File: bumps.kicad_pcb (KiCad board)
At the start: 2 copper layers, 111.1 x 65.4 mm, 132 parts, among them M1 CONN_1, M2 CONN_1, M3 CONN_1, P1 DIL6, P10 Mot-A, P11 Mot-A, P12 Mot-X, P13 T1, P14 T2, P15 T3, P16 MPower, P17 PWM-2, P18 PWM-1, P19 END-X, P2 DIL6, P20 END-Y, P21 END-Z, P22 Mot-X, P23 Mot-Y, P24 Mot-Y, P25 Mot-Z, P26 Mot-Z, P27 Aux, P29 PWM, P3 Mot-E, P4 Mot-E, P5 DIL6, P6 DIL6, P7 DIL6, P8 P8 Header, P9 P9 Header, Q1 IRLB8743PBF, Q2 IRLB8743PBF, Q3 FDS9926A, Q4 FDS9926A, U1 E-Polo, U2 A-Polo, U3 X-Polo, U4 Y-Polo, U5 Z-Polo, U6 MC34063, U7 AP1117/3.3

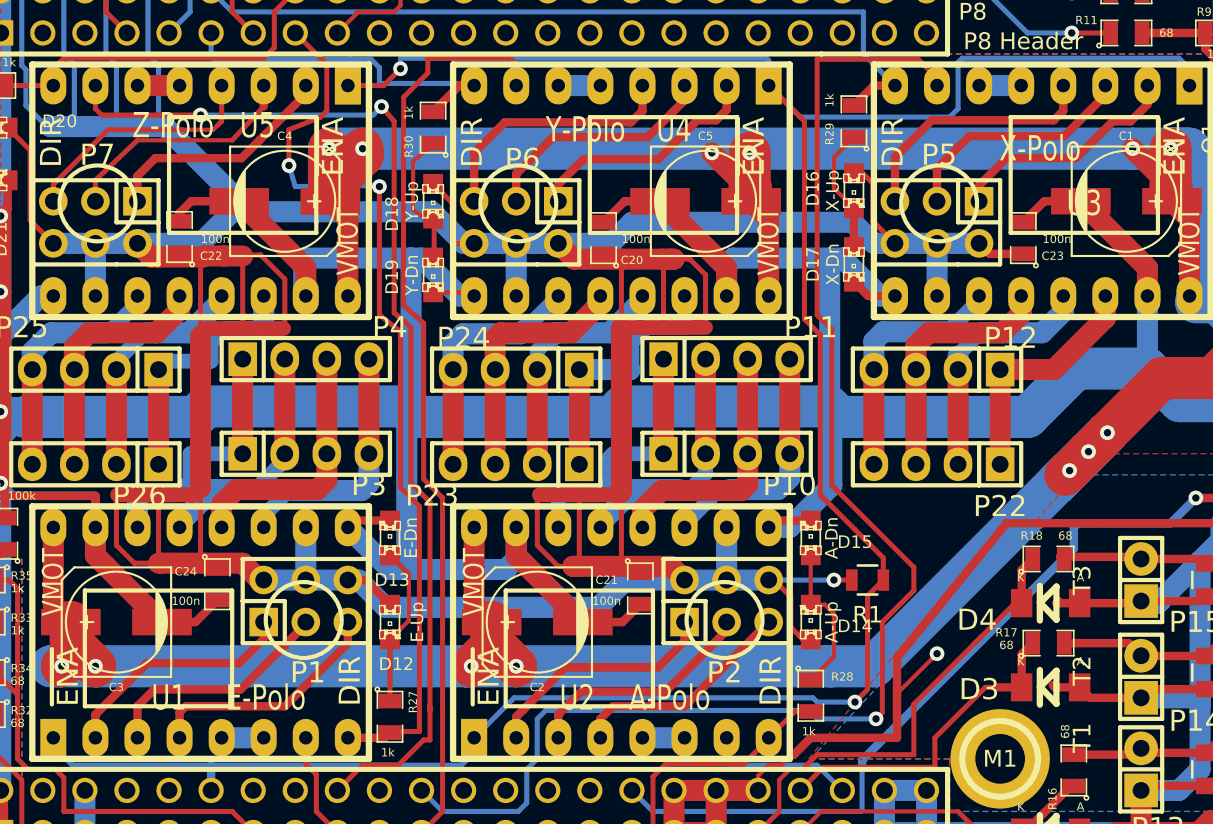
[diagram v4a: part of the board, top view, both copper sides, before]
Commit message: o Rename motor labels from 'Polo X' to 'Motor 1'. The axis assignment   is not done in the hardware, but can be freely assigned in the   software. So this would be confusing.
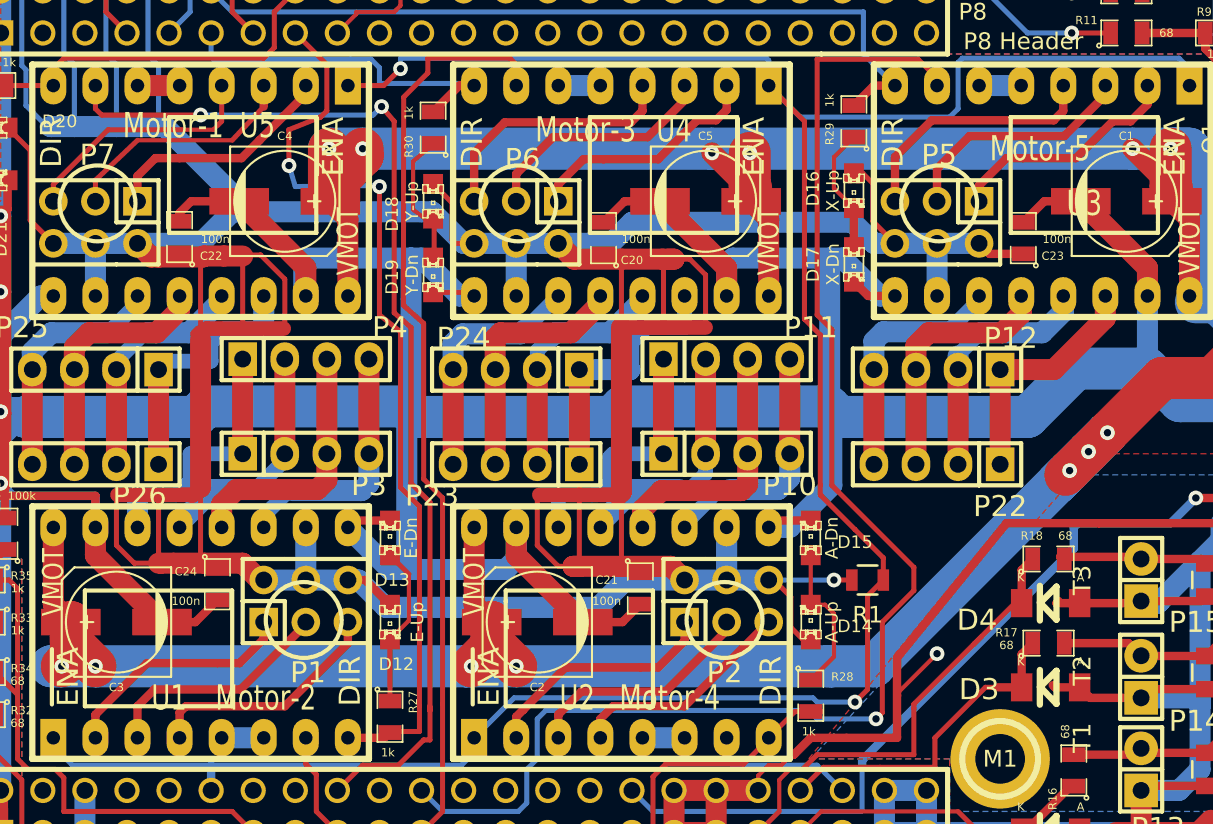
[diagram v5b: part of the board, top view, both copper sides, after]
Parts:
- U1: value E-Polo -> Motor-2
- U2: value A-Polo -> Motor-4
- U3: value X-Polo -> Motor-5
- U4: value Y-Polo -> Motor-3
- U5: value Z-Polo -> Motor-1
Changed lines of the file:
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@@
       (effects (font (size 1.524 1.143) (thickness 0.3048)))
     )
-    (fp_text value E-Polo (at 3.937 1.397) (layer F.SilkS)
+    (fp_text value Motor-2 (at 3.937 1.397) (layer F.SilkS)
       (effects (font (size 1.524 1.143) (thickness 0.3048)))
     )
@@
       (effects (font (size 1.524 1.143) (thickness 0.3048)))
     )
-    (fp_text value A-Polo (at 2.921 1.397) (layer F.SilkS)
+    (fp_text value Motor-4 (at 2.921 1.397) (layer F.SilkS)
       (effects (font (size 1.524 1.143) (thickness 0.3048)))
     )
@@
       (effects (font (size 1.524 1.143) (thickness 0.3048)))
     )
-    (fp_text value X-Polo (at 0.127 0 180) (layer F.SilkS)
+    (fp_text value Motor-5 (at 0.127 0 180) (layer F.SilkS)
       (effects (font (size 1.524 1.143) (thickness 0.3048)))
     )
@@
       (effects (font (size 1.524 1.143) (thickness 0.3048)))
     )
-    (fp_text value Y-Polo (at 2.159 1.143 180) (layer F.SilkS)
+    (fp_text value Motor-3 (at 2.159 1.143 180) (layer F.SilkS)
       (effects (font (size 1.524 1.143) (thickness 0.3048)))
     )
@@
       (effects (font (size 1.524 1.143) (thickness 0.3048)))
     )
-    (fp_text value Z-Polo (at 1.651 1.397 180) (layer F.SilkS)
-      (effects (font (size 1.524 1.143) (thickness 0.3048)))
-    )
+    (fp_text value Motor-1 (at 1.651 1.397 180) (layer F.SilkS)
+      (effects (font (size 1.524 1.143) (thickness 0.3048)))
+    )

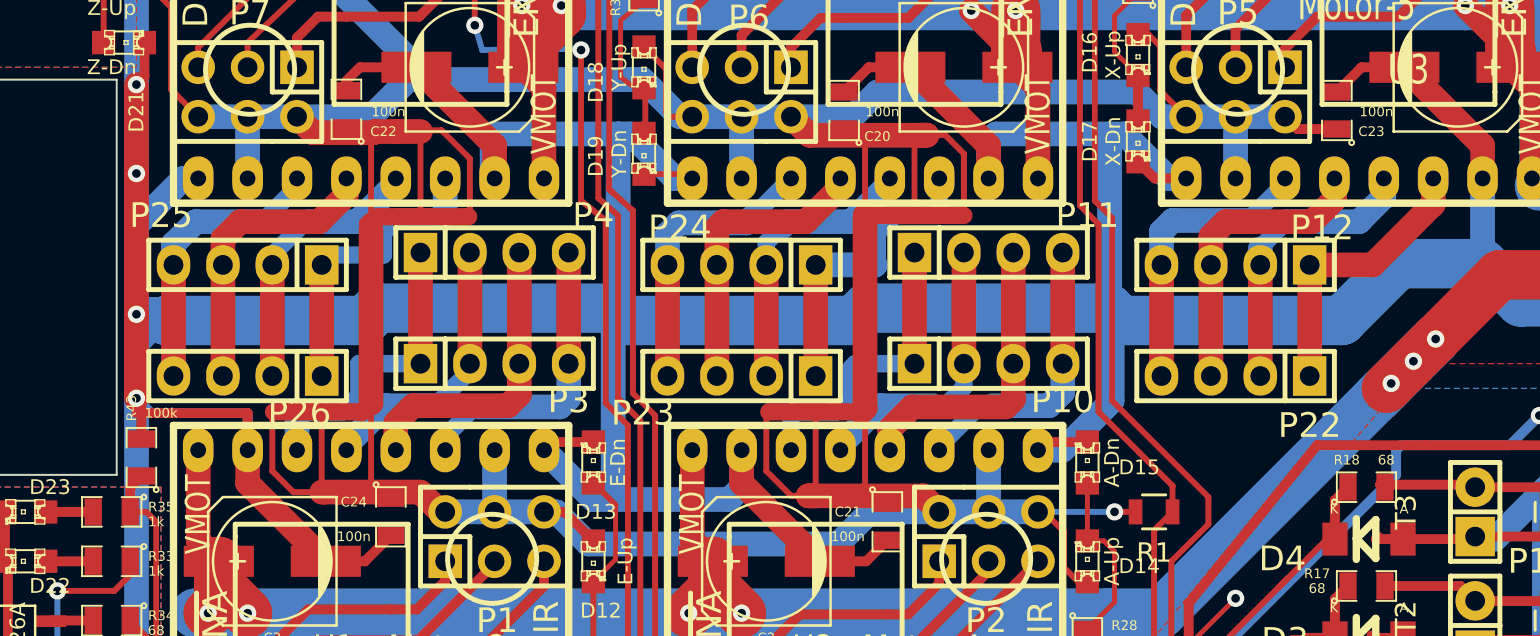
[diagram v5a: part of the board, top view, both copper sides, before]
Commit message: o Put all motor connectors in a line (not wiggly line anymore) o Have distance between the same motor connectors 0.2" (distance in female   dual sided edge connector) o Fixes #5
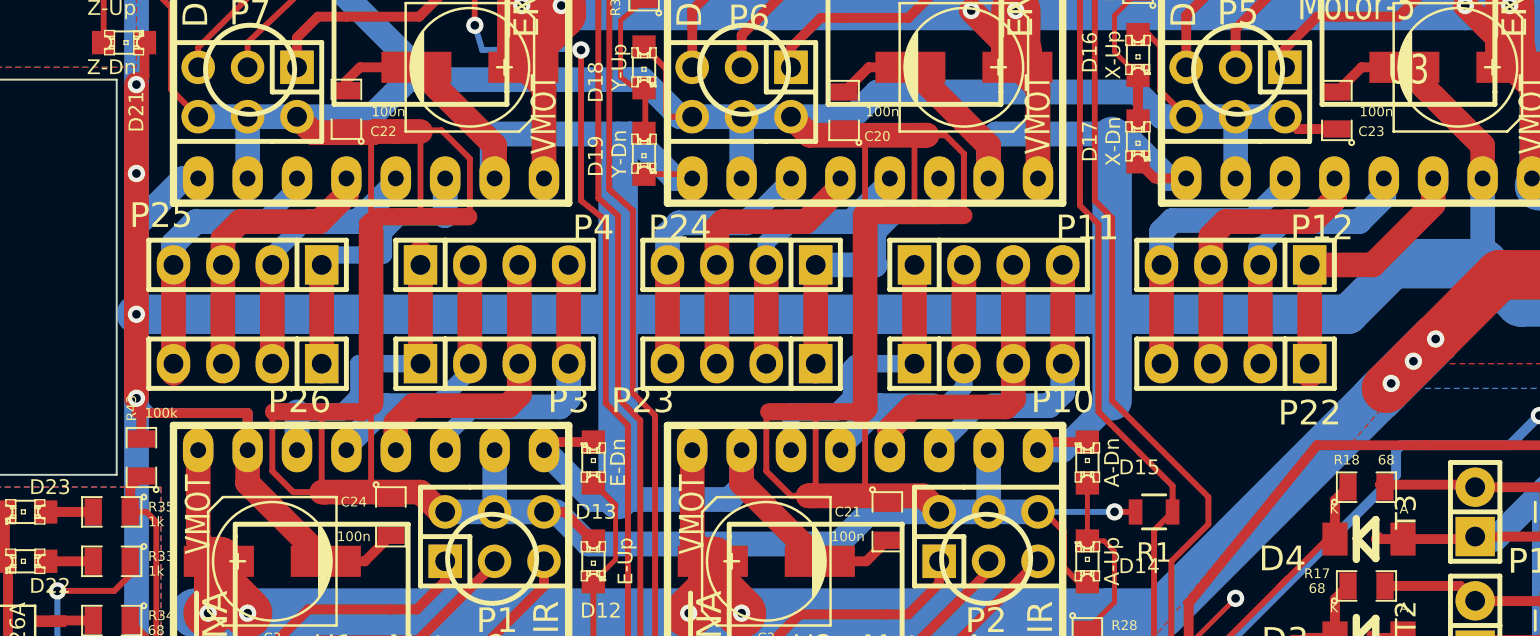
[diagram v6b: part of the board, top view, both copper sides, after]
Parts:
- moved P11 0.63 mm to (104.8, 62.2)
- moved P4 0.63 mm to (79.4, 62.2)
- moved P22 0.63 mm to (117.5, 67.3)
- moved P23 0.63 mm to (92.1, 67.3)
- moved P26 0.63 mm to (66.7, 67.3)
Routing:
- net GND: track 826.8 -> 819.3 mm

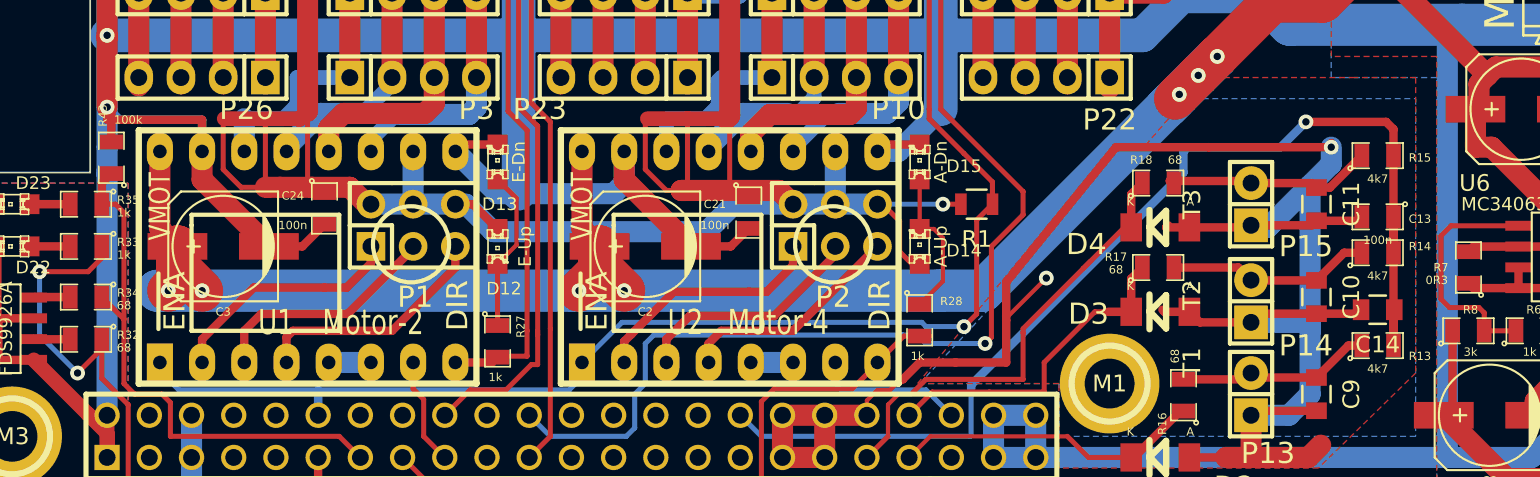
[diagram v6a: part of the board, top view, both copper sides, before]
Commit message: o straighten some traces, and user thicker traces where possible.
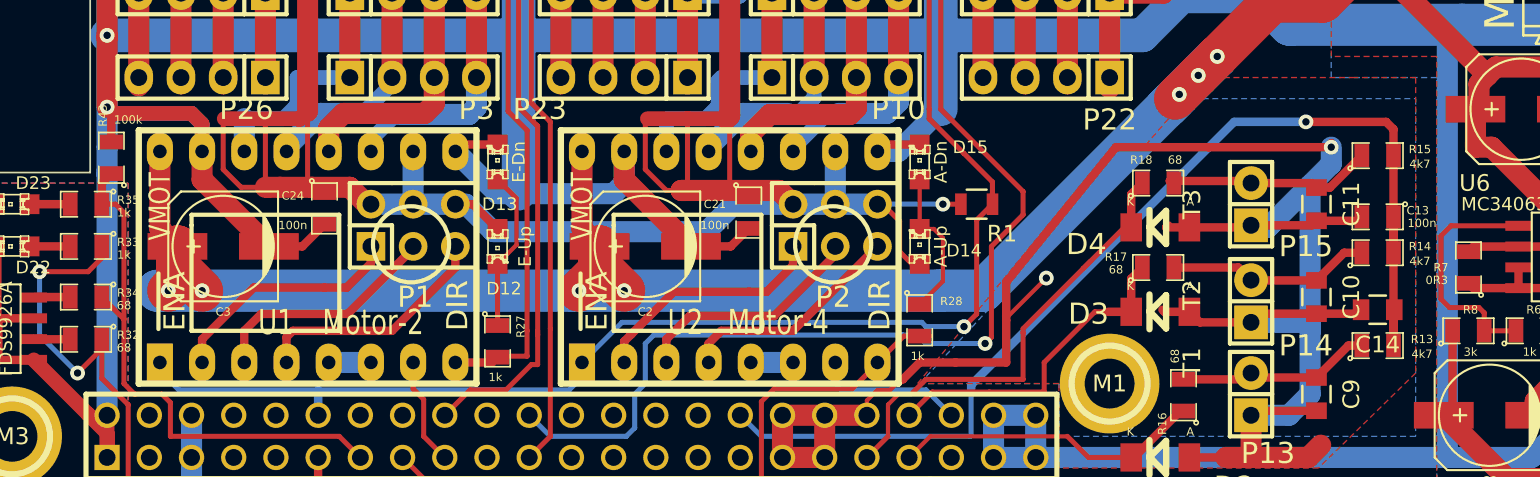
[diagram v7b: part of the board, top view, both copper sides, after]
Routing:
- net VDD_ADC: track 67.9 -> 67.1 mm

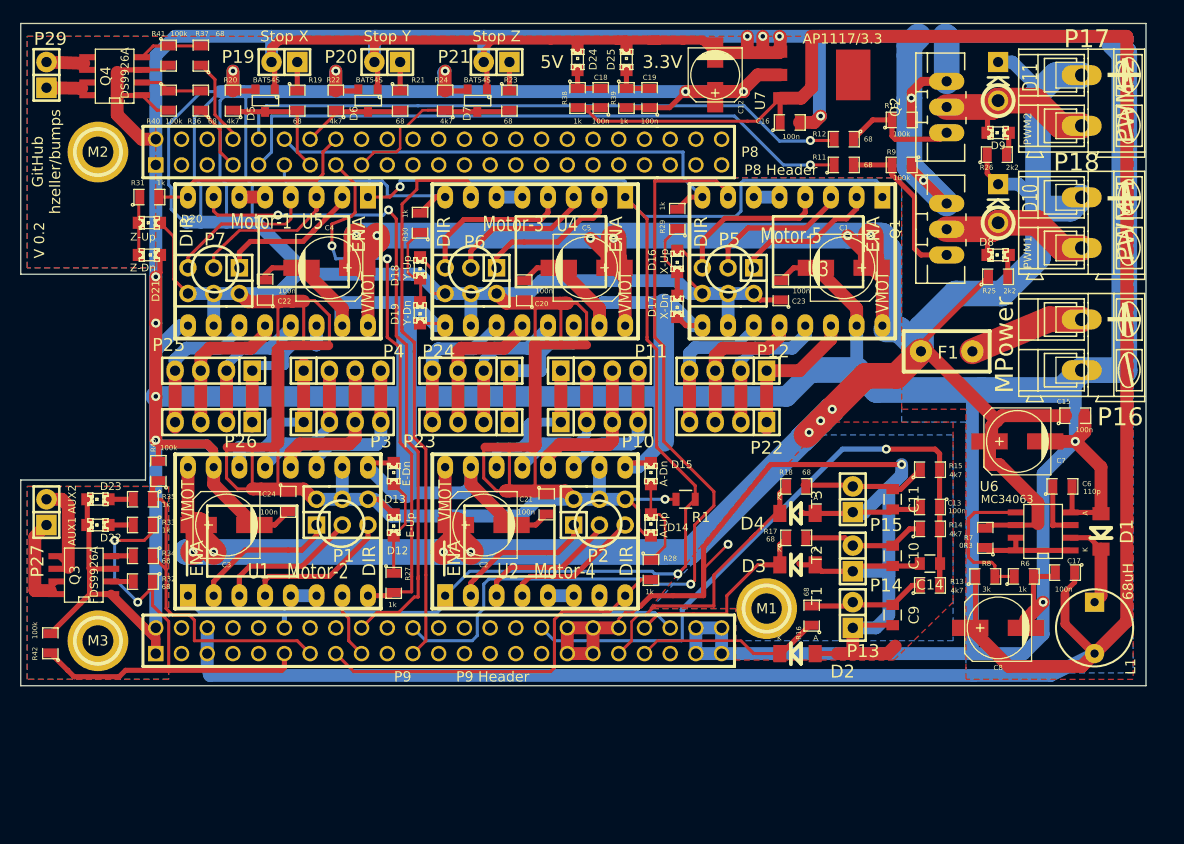
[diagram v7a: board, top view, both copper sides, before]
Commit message: o convert library to .pretty o add DIL-4 for OptoCoupler (Didn't find it in lib?) and 0.2" distance   Wide header for the Estop switch. o assignement and import into pcb, but not routed yet. o make a bit more space to add another end-switch (the visual glitch detector   capacitors on the LEDs had to go).
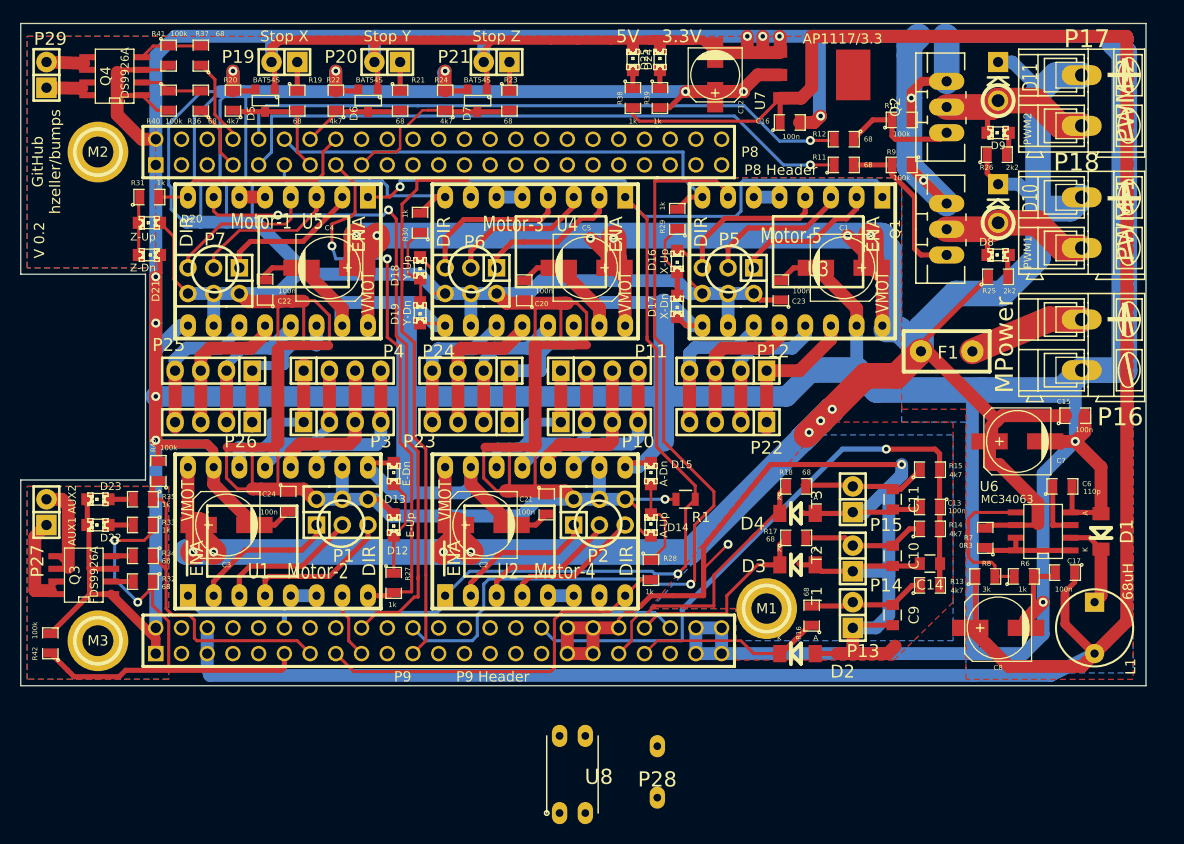
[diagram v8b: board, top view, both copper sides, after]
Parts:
- removed C18, C19: 100n, SMD_Packages:SM0805
- added P28: KillSwitch, bumps:WideHeader, F.Cu at (110.5, 101.9)
- added U8: Opto, bumps:DIL-4, F.Cu at (102.1, 102.1)
- moved D24 5.46 mm to (108.1, 31.5)
- moved R38 5.46 mm to (108.1, 35.3)
- moved D25 3.30 mm to (110.7, 31.5)
- moved R39 3.30 mm to (110.7, 35.3)
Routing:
- net VDD_5V: track 249.3 -> 242.8 mm
- net VDD_3V3: track 449.2 -> 445.9 mm
- net GND: track 819.3 -> 822.6 mm
- net Net-(D25-Pad1): track 4.09 -> 1.81 mm
- net Net-(D24-Pad1): track 4.09 -> 1.81 mm
